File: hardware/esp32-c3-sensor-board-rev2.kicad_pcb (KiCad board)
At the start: 2 copper layers, 46 x 89 mm, 14 parts, among them J1 BME280_Module, J2 BH1750_Module, J3 Relay, J4 Button, J5 BREAKOUT, U1 ESP32-C3-SuperMini, U2 HLK-LD2410C

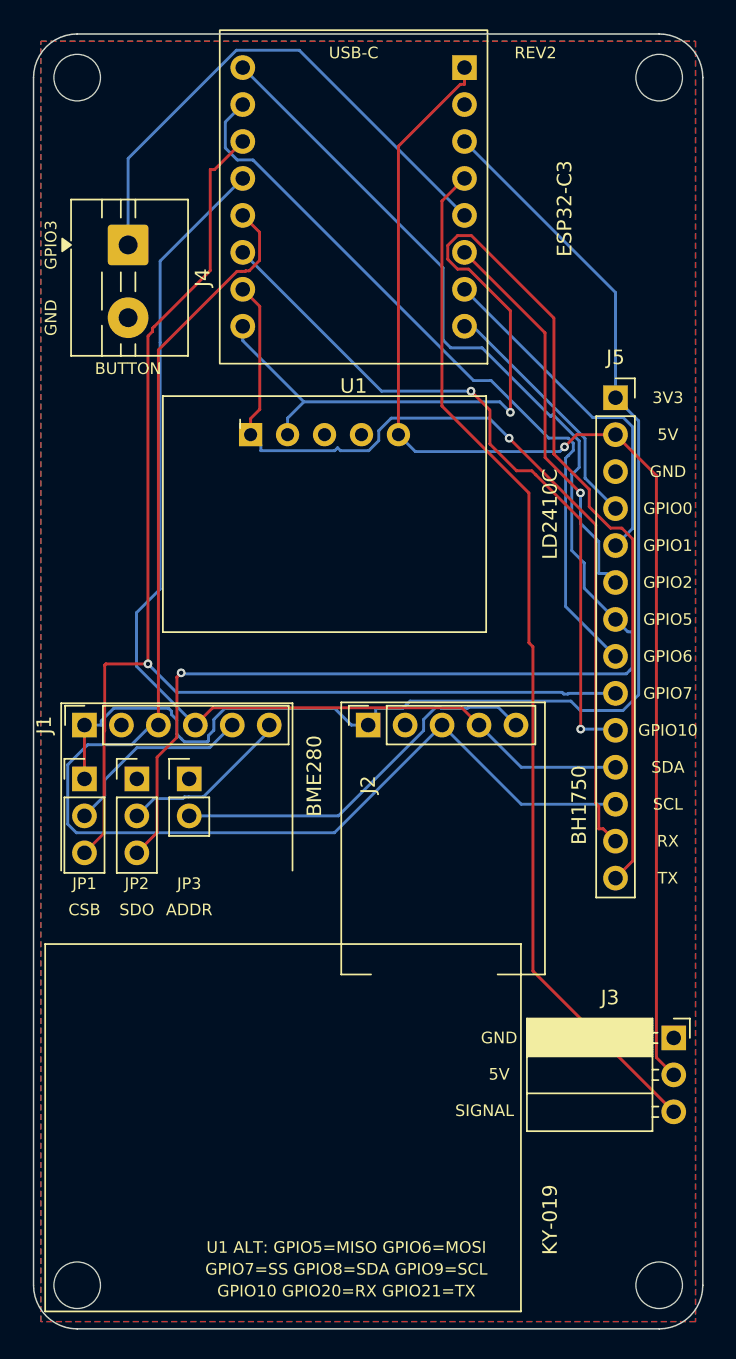
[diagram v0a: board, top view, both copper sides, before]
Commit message: Enlarge vias to 0.8 mm for AISLER annular-ring rule
AISLER's 2L 1.6 mm 35 um process requires a 200 um via annular ring
(175 um absolute minimum if the 0.3 mm drill is widened to 0.45 mm).
The board's 0.6/0.3 mm vias gave only 150 um, which failed the upload
check. Re-routed with 0.8/0.3 mm vias (250 um nominal ring), widened
silkscreen to AISLER's 0.15 mm minimum, and regenerated gerbers/drill.

DRC: 0 errors, 0 unconnected, 2 cosmetic silk warnings. ERC: 0.

Co-Authored-By: Claude Code <noreply@anthropic.com>
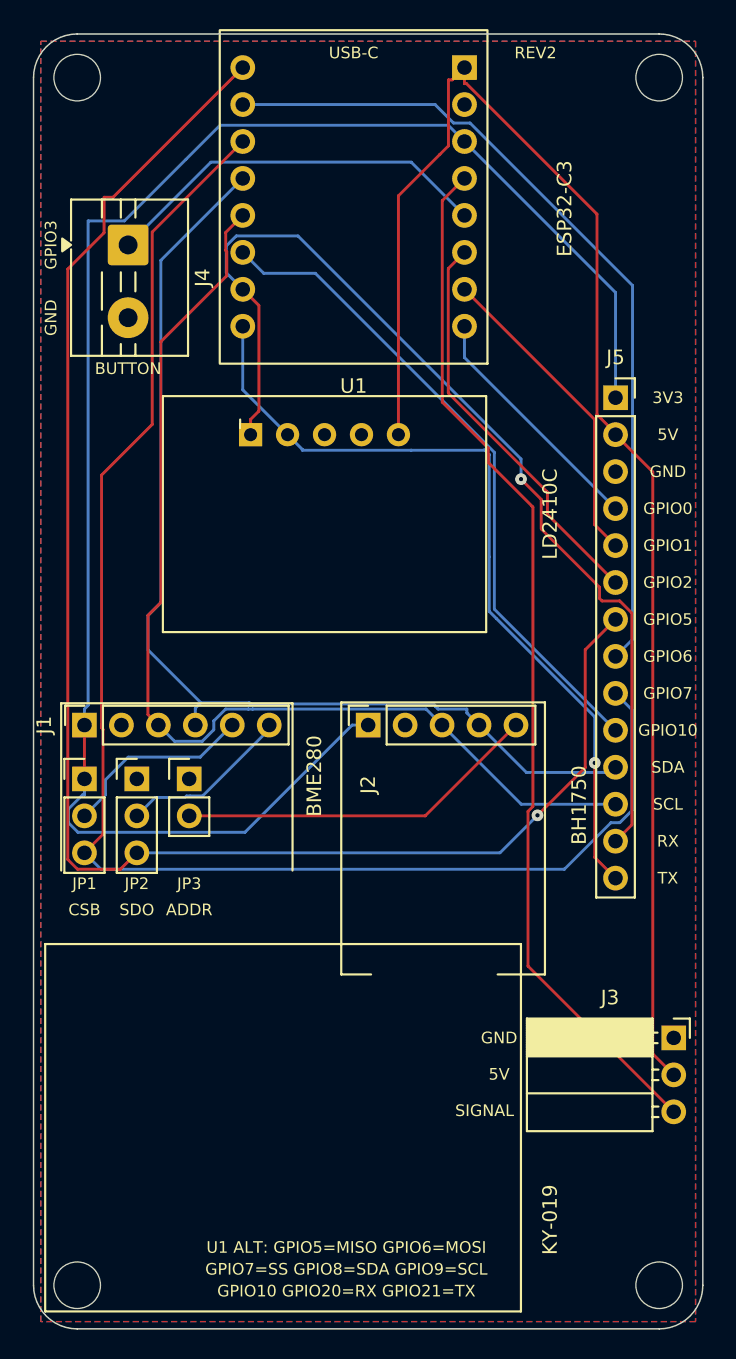
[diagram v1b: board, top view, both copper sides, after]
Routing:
- net UART_TX: track 89.5 -> 55.9 mm
- net 3V3: track 90.9 -> 116.9 mm
- net I2C_SCL: track 93.5 -> 74.0 mm
- net 5V: track 88.8 -> 102.5 mm, vias 1 -> 0
- net SPI_CS: track 88.3 -> 101.8 mm, vias 1 -> 0
- net SPI_MISO: track 99.4 -> 109.5 mm
- net BUTTON: track 36.8 -> 27.0 mm
- net UART_RX: track 62.2 -> 71.6 mm
- net IO6: track 52.1 -> 57.9 mm
- net IO10: track 49.0 -> 45.5 mm, vias 2 -> 0
- net IO1: track 24.1 -> 21.9 mm
- net BH_ADDR: track 26.6 -> 25.0 mm
- net IO2: track 27.3 -> 27.9 mm, vias 1 -> 0
- net I2C_SDA: track 73.3 -> 72.7 mm

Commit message: Route with 0.25 mm traces and 0.20 mm clearance
The 0.20/0.15 mm board met AISLER's published minima but their own
2-layer simple DRC template uses 0.20 mm clearance, which flagged 63
clearance items. Re-routed with 0.25 mm traces, 0.20 mm clearance and
0.8/0.3 mm vias (0.25 mm annular), and set the project rules to those
values. Copper-to-edge is 0.354 mm (AISLER min 0.30).

Verified with AISLER's exact 2-layer-simple project rules + .kicad_dru:
0 errors. Own DRC: 0 errors / 0 unconnected (2 cosmetic silk warnings).
ERC: 0. Gerbers/drill/zip regenerated; copper apertures C0.25/C0.8,
silk C0.15, drill min 0.3 mm.

Co-Authored-By: Claude Code <noreply@anthropic.com>
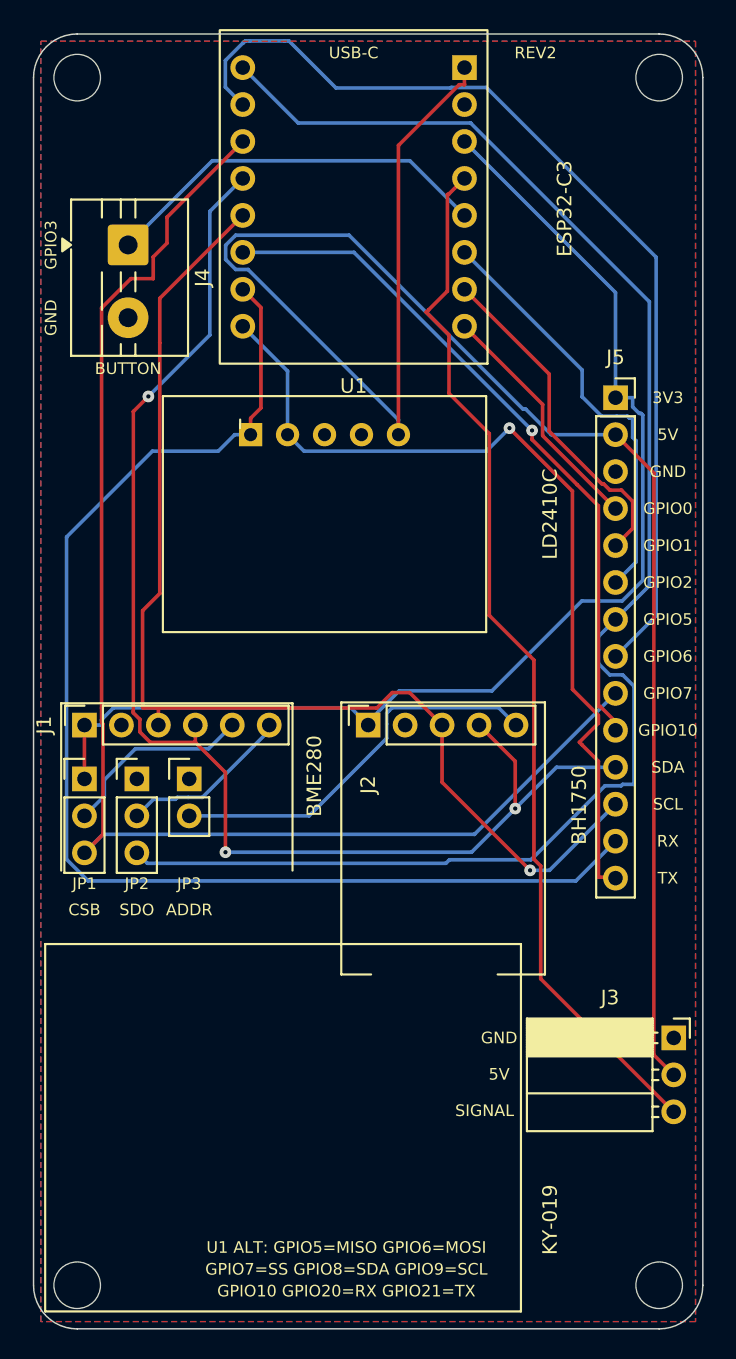
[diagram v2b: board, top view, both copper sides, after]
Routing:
- net 3V3: track 116.9 -> 83.5 mm
- net 5V: track 102.5 -> 124.2 mm
- net I2C_SDA: track 72.7 -> 91.0 mm, vias 0 -> 3
- net UART_RX: track 71.6 -> 88.0 mm, vias 1 -> 0
- net IO6: track 57.9 -> 68.5 mm
- net SPI_CS: track 101.8 -> 95.4 mm
- net I2C_SCL: track 74.0 -> 80.0 mm, vias 0 -> 1
- net UART_TX: track 55.9 -> 60.8 mm
- net IO10: track 45.5 -> 48.0 mm, vias 0 -> 1
- net SPI_MISO: track 109.5 -> 107.5 mm, vias 1 -> 0
- net BH_ADDR: track 25.0 -> 27.0 mm
- net IO1: track 21.9 -> 23.4 mm
- net IO2: track 27.9 -> 29.3 mm
- net RELAY: track 71.7 -> 72.3 mm

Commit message: Untent vias and clear silk from pads for AISLER
AISLER's 2L 1.6 mm 35 um process does not support tented vias or
silkscreen on pads. Both had been present on every version, so the
upload error never changed.

- Disable via tenting (board + per-via); mask layers now carry 0.9 mm
  via openings (0.8 mm via + 50 um mask expansion).
- Set 50 um solder-mask expansion; 0.125 mm silk clearance rule.
- Move U2 pin-1 silk marker 0.4 mm off pad 1 and update the library
  footprint to match.
- Regenerate gerbers/drill/zip.

AISLER's exact 2-layer-simple rules + .kicad_dru: 0 errors.
Own DRC: 0 errors / 0 unconnected (26 cosmetic silk warnings).
ERC: 0.

Co-Authored-By: Claude Code <noreply@anthropic.com>
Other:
- rule pad_to_mask_clearance: 0 -> 0.05
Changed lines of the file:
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@@
 	)
 	(setup
-		(pad_to_mask_clearance 0)
+		(pad_to_mask_clearance 0.05)
 		(allow_soldermask_bridges_in_footprints no)
 		(tenting
-			(front yes)
-			(back yes)
+			(front no)
+			(back no)
 		)
 		(covering
@@
 		)
 		(fp_line
-			(start -5.8 -6.5)
-			(end -5.8 -5.9)
+			(start -6.2 -6.5)
+			(end -6.2 -5.9)
 			(stroke
 				(width 0.15)
@@
 		(drill 0.3)
 		(layers "F.Cu" "B.Cu")
+		(tenting
+			(front no)
+			(back no)
+		)
 		(net "UART_TX")
 	)
@@
 		(drill 0.3)
 		(layers "F.Cu" "B.Cu")
+		(tenting
+			(front no)
+			(back no)
+		)
 		(net "I2C_SCL")
 	)
@@
 		(drill 0.3)
 		(layers "F.Cu" "B.Cu")
+		(tenting
+			(front no)
+			(back no)
+		)
 		(net "I2C_SDA")
 	)
@@
 		(drill 0.3)
 		(layers "F.Cu" "B.Cu")
+		(tenting
+			(front no)
+			(back no)
+		)
 		(net "I2C_SDA")
 	)
@@
 		(drill 0.3)
 		(layers "F.Cu" "B.Cu")
+		(tenting
+			(front no)
+			(back no)
+		)
 		(net "I2C_SDA")
 	)
@@
 		(drill 0.3)
 		(layers "F.Cu" "B.Cu")
+		(tenting
+			(front no)
+			(back no)
+		)
 		(net "IO10")
 	)
